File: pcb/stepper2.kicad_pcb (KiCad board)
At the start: 2 copper layers, 92 x 138 mm, 52 parts, among them J1 DA15_Receptacle_MountingHoles, J10 Conn_01x07_Pin, J11 FAN, J2 DA15_Receptacle_MountingHoles, J3 DA15_Receptacle_MountingHoles, J4 DE15_Receptacle_HighDensity, J5 DE15_Receptacle_HighDensity, J6 DE15_Receptacle_HighDensity, J7 Conn_01x04_Pin, J8 Conn_01x05_Pin, J9 Conn_01x06_Pin, SW1 SW_Push, SW2 SW_Push, SW3 SW_Push, SW4 SW_Push, SW5 SW_Push, SW6 SW_Push, U1 AM26LS32ACN, U2 AM26LS32Ax, U3 AM26LS32ACN, U4 TMC2209_BIGTREETECH, U5 TMC2209_BIGTREETECH, U6 TMC2209_BIGTREETECH

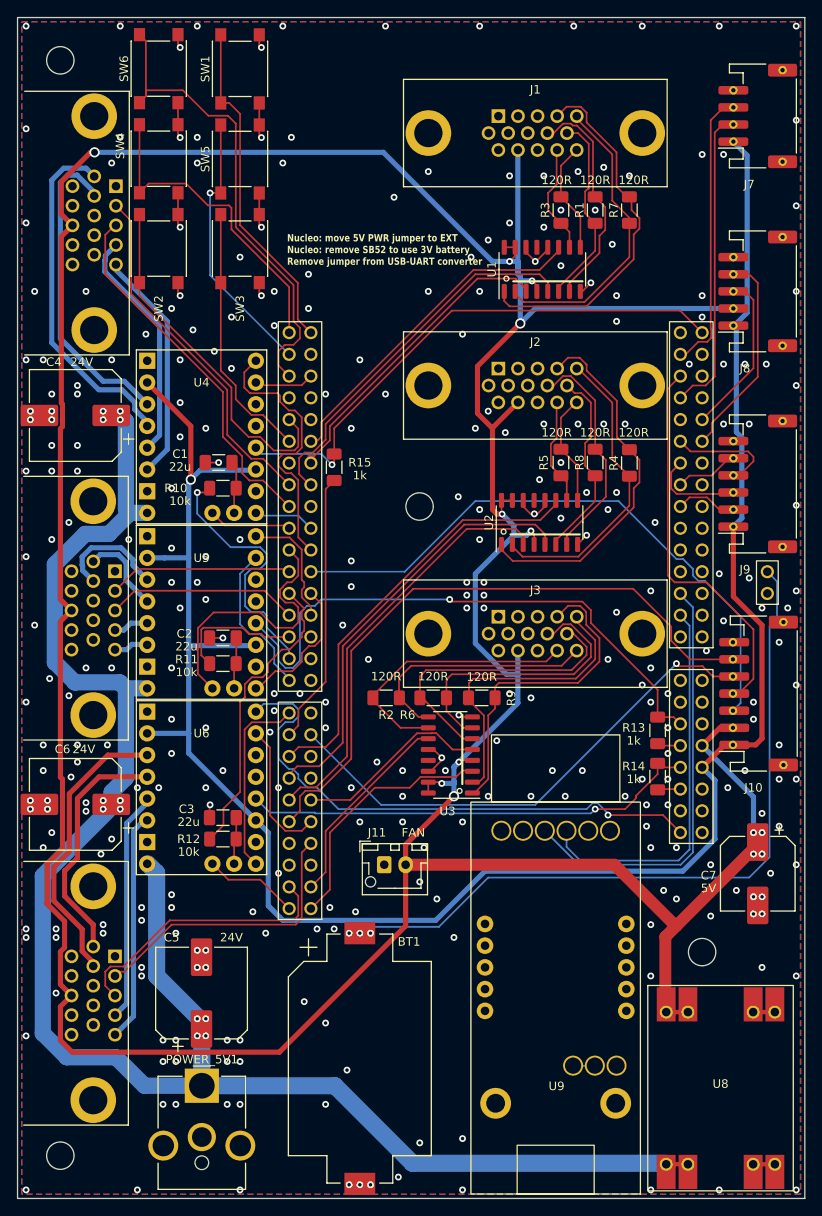
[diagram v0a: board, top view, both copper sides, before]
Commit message: PCB - adjustments and author/date label
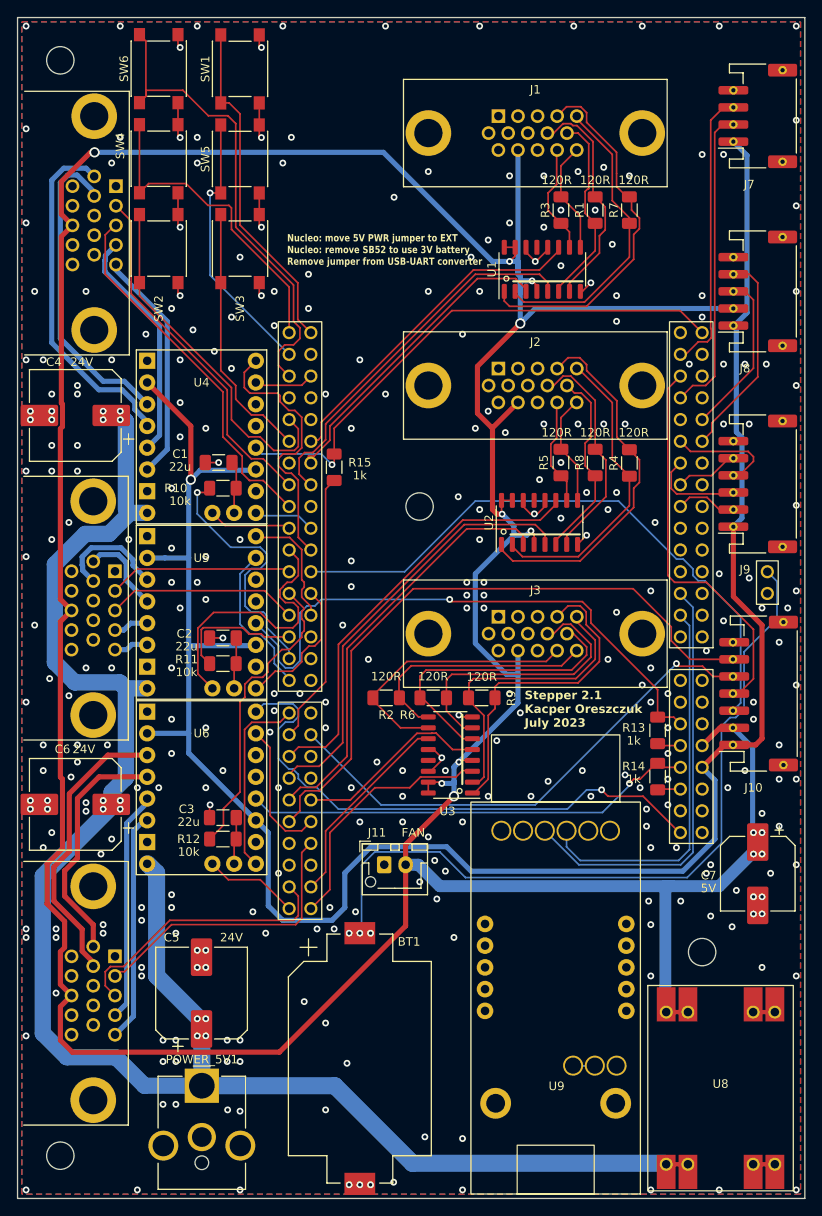
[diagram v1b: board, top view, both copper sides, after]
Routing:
- net +3V3: track 240.5 -> 245.2 mm
- net VBAT: track 88.4 -> 91.8 mm
- net +5V: track 456.3 -> 459.6 mm
- net DIR3: track 64.4 -> 65.5 mm
- net TMCUART3: track 53.9 -> 53.0 mm
- net GND: vias 307 -> 311
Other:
- board text added: "Stepper 2.1 Kacper Oreszczuk July 2023"

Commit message: PCB - minor tweaks
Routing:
- net +5V: track 459.6 -> 458.4 mm
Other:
- board text added: "Remove jumper from USB-UART converter Nucleo: move 5V PWR jumper to EXT Nucleo: remove SB52 to use 3V battery"
- board text removed: "Nucleo: move 5V PWR jumper to EXT Nucleo: remove SB52 to use 3V battery Remove jumper from USB-UART converter"
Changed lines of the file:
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@@
     (property "ki_keywords" "R res resistor")
     (attr smd)
-    (fp_text reference "R5" (at 0 -2 270) (layer "F.SilkS")
+    (fp_text reference "R5" (at 1.5 -3.25) (layer "F.SilkS")
         (effects (font (size 1 1) (thickness 0.15)))
     )
-    (fp_text value "120R" (at 3.5 -0.5 180) (layer "F.SilkS")
+    (fp_text value "120R" (at 0 -3.25 180) (layer "F.SilkS")
         (effects (font (size 1 1) (thickness 0.15)))
     )
@@
     (property "ki_keywords" "R res resistor")
     (attr smd)
-    (fp_text reference "R7" (at 0 -1.82 90) (layer "F.SilkS")
+    (fp_text reference "R7" (at 1.25 3.25 180) (layer "F.SilkS")
         (effects (font (size 1 1) (thickness 0.15)))
     )
-    (fp_text value "120R" (at 3.5 0.5 180) (layer "F.SilkS")
+    (fp_text value "120R" (at -0.5 3.25 180) (layer "F.SilkS")
         (effects (font (size 1 1) (thickness 0.15)))
     )
@@
         (effects (font (size 1 1) (thickness 0.15)))
     )
-    (fp_text value "120R" (at 3.5 0 180) (layer "F.SilkS")
+    (fp_text value "120R" (at 0 2 270) (layer "F.SilkS")
         (effects (font (size 1 1) (thickness 0.15)))
     )
@@
     (property "ki_keywords" "R res resistor")
     (attr smd)
-    (fp_text reference "R2" (at 0 2) (layer "F.SilkS")
+    (fp_text reference "R2" (at -4.075 -2) (layer "F.SilkS")
         (effects (font (size 1 1) (thickness 0.15)))
     )
-    (fp_text value "120R" (at 0 -2.5) (layer "F.SilkS")
+    (fp_text value "120R" (at -4.075 -0.5) (layer "F.SilkS")
         (effects (font (size 1 1) (thickness 0.15)))
     )
@@
     (property "ki_keywords" "R res resistor")
     (attr smd)
-    (fp_text reference "R9" (at 3.45 0.05 90) (layer "F.SilkS")
+    (fp_text reference "R9" (at 2.25 1.75 180) (layer "F.SilkS")
         (effects (font (size 1 1) (thickness 0.15)))
     )
-    (fp_text value "120R" (at 0 -2.45) (layer "F.SilkS")
+    (fp_text value "120R" (at 2.25 3.25) (layer "F.SilkS")
         (effects (font (size 1 1) (thickness 0.15)))
     )
@@
     (property "ki_keywords" "R res resistor")
     (attr smd)
-    (fp_text reference "R3" (at 0 -1.82 90) (layer "F.SilkS")
+    (fp_text reference "R3" (at 1.75 -3.25 180) (layer "F.SilkS")
         (effects (font (size 1 1) (thickness 0.15)))
     )
-    (fp_text value "120R" (at 3.5 -0.5 180) (layer "F.SilkS")
+    (fp_text value "120R" (at 0 -3.25 180) (layer "F.SilkS")
         (effects (font (size 1 1) (thickness 0.15)))
     )
@@
     (property "ki_keywords" "R res resistor")
     (attr smd)
-    (fp_text reference "R6" (at -3 2) (layer "F.SilkS")
+    (fp_text reference "R6" (at -3.325 2) (layer "F.SilkS")
         (effects (font (size 1 1) (thickness 0.15)))
     )
-    (fp_text value "120R" (at 0 -2.5) (layer "F.SilkS")
+    (fp_text value "120R" (at -3.575 3.25) (layer "F.SilkS")
         (effects (font (size 1 1) (thickness 0.15)))
     )
@@
     (property "ki_keywords" "R res resistor")
     (attr smd)
-    (fp_text reference "R4" (at 0 -1.82 90) (layer "F.SilkS")
+    (fp_text reference "R4" (at -3.2 1.75 180) (layer "F.SilkS")
         (effects (font (size 1 1) (thickness 0.15)))
     )
-    (fp_text value "120R" (at 3.55 0.5 180) (layer "F.SilkS")
+    (fp_text value "120R" (at -4.7 2 180) (layer "F.SilkS")
         (effects (font (size 1 1) (thickness 0.15)))
     )
@@
     (property "ki_keywords" "R res resistor")
     (attr smd)
-    (fp_text reference "R8" (at 0 -1.82 90) (layer "F.SilkS")
+    (fp_text reference "R8" (at -3.5 0.75 180) (layer "F.SilkS")
         (effects (font (size 1 1) (thickness 0.15)))
     )
-    (fp_text value "120R" (at 3.5 0 180) (layer "F.SilkS")
+    (fp_text value "120R" (at -5 0.75) (layer "F.SilkS")
         (effects (font (size 1 1) (thickness 0.15)))
     )
@@
   (gr_line (start 0 138) (end 0 0)
     (stroke (width 0.1) (type default)) (layer "Edge.Cuts"))
-  (gr_text "Nucleo: move 5V PWR jumper to EXT\nNucleo: remove SB52 to use 3V battery\nRemove jumper from USB-UART converter" (at 31.5 29) (layer "F.SilkS")
-    (effects (font (size 0.85 0.7) (thickness 0.175) bold) (justify left bottom))
+  (gr_text "Remove jumper from USB-UART converter\nNucleo: move 5V PWR jumper to EXT\nNucleo: remove SB52 to use 3V battery" (at 30 28.5) (layer "F.SilkS")
+    (effects (font (size 0.85 0.85) (thickness 0.175) bold) (justify left bottom))
   )
   (gr_text "Stepper 2.1\nKacper Oreszczuk\nJuly 2023" (at 59.25 83) (layer "F.SilkS")
@@
   (via (at 18.5 107) (size 0.8) (drill 0.4) (layers "F.Cu" "B.Cu") (free) (net 2))
   (via (at 82 137) (size 0.8) (drill 0.4) (layers "F.Cu" "B.Cu") (free) (net 2))
-  (via (at 69 57.5) (size 0.8) (drill 0.4) (layers "F.Cu" "B.Cu") (free) (net 2))
+  (via (at 69 58.25) (size 0.8) (drill 0.4) (layers "F.Cu" "B.Cu") (free) (net 2))
   (via (at 11 40) (size 0.8) (drill 0.4) (layers "F.Cu" "B.Cu") (free) (net 2))
   (via (at 85.5 47.5) (size 0.8) (drill 0.4) (layers "F.Cu" "B.Cu") (free) (net 2))
@@
   (via (at 26 61) (size 0.8) (drill 0.4) (layers "F.Cu" "B.Cu") (free) (net 2))
   (via (at 28.5 24.5) (size 0.8) (drill 0.4) (layers "F.Cu" "B.Cu") (net 2))
-  (via (at 53 28) (size 0.8) (drill 0.4) (layers "F.Cu" "B.Cu") (free) (net 2))
+  (via (at 52.25 29) (size 0.8) (drill 0.4) (layers "F.Cu" "B.Cu") (free) (net 2))
   (via (at 82.5 16) (size 0.8) (drill 0.4) (layers "F.Cu" "B.Cu") (free) (net 2))
   (via (at 6.25 88.75) (size 0.8) (drill 0.4) (layers "F.Cu" "B.Cu") (free) (net 2))
@@
   (via (at 18 55) (size 0.8) (drill 0.4) (layers "F.Cu" "B.Cu") (free) (net 2))
   (via (at 1 63) (size 0.8) (drill 0.4) (layers "F.Cu" "B.Cu") (free) (net 2))
-  (via (at 55 26) (size 0.8) (drill 0.4) (layers "F.Cu" "B.Cu") (free) (net 2))
+  (via (at 55.5 26.75) (size 0.8) (drill 0.4) (layers "F.Cu" "B.Cu") (free) (net 2))
   (via (at 54 61) (size 0.8) (drill 0.4) (layers "F.Cu" "B.Cu") (free) (net 2))
   (via (at 4 50) (size 0.8) (drill 0.4) (layers "F.Cu" "B.Cu") (free) (net 2))
@@
   (segment (start 62 22.55) (end 63.5 24.05) (width 0.2) (layer "F.Cu") (net 36))
   (segment (start 64.5 25.05) (end 63.5 24.05) (width 0.2) (layer "F.Cu") (net 36))
-  (segment (start 65.77 26.85) (end 65.77 23.22) (width 0.2) (layer "F.Cu") (net 37))
+  (segment (start 65.25 24) (end 65.25 22.5) (width 0.2) (layer "F.Cu") (net 37))
   (segment (start 63.5 20.95) (end 63.5 17.325001) (width 0.2) (layer "F.Cu") (net 37))
-  (segment (start 65.77 23.22) (end 63.5 20.95) (width 0.2) (layer "F.Cu") (net 37))
+  (segment (start 65.77 26.85) (end 65.77 24.52) (width 0.2) (layer "F.Cu") (net 37))
+  (segment (start 65.77 24.52) (end 65.25 24) (width 0.2) (layer "F.Cu") (net 37))
+  (segment (start 65.25 22.5) (end 63.7 20.95) (width 0.2) (layer "F.Cu") (net 37))
+  (segment (start 63.7 20.95) (end 63.5 20.95) (width 0.2) (layer "F.Cu") (net 37))
   (segment (start 63.5 17.325001) (end 65.345001 15.48) (width 0.2) (layer "F.Cu") (net 37))
   (segment (start 72 55) (end 72 57.25) (width 0.2) (layer "F.Cu") (net 38))
@@
   (segment (start 51.765 86.81) (end 51.575 87) (width 0.2) (layer "F.Cu") (net 142))
   (segment (start 56.0255 58.0255) (end 55.5 57.5) (width 0.6) (layer "F.Cu") (net 142))
-  (segment (start 86.5 96.35) (end 86.5 96.628882) (width 1.4) (layer "F.Cu") (net 142))
   (segment (start 58.15 27.85) (end 58.15 26.85) (width 0.2) (layer "F.Cu") (net 142))
   (segment (start 53.15 86.81) (end 51.765 86.81) (width 0.2) (layer "F.Cu") (net 142))
@@
   (segment (start 60.69 32) (end 60.69 31.336602) (width 0.2) (layer "F.Cu") (net 142))
   (segment (start 5.00772 70.585) (end 5.00772 88.75386) (width 0.6) (layer "F.Cu") (net 142))
-  (segment (start 75.7 116.12) (end 75.8 116.22) (width 1.4) (layer "F.Cu") (net 142))
   (segment (start 53.745001 46.245001) (end 53.745001 40.754999) (width 0.6) (layer "F.Cu") (net 142))
   (segment (start 5.12 25.585) (end 5.12 45.05934) (width 0.6) (layer "F.Cu") (net 142))
@@
   (via (at 58.75 35.75) (size 1.2) (drill 0.8) (layers "F.Cu" "B.Cu") (net 142))
   (segment (start 58.475001 28.5) (end 58.475001 29.975001) (width 0.6) (layer "B.Cu") (net 142))
-  (segment (start 76.5 101.5) (end 75.7 101.5) (width 1.4) (layer "B.Cu") (net 142))
   (segment (start 57.116523 76.75) (end 53.5 73.133477) (width 0.6) (layer "B.Cu") (net 142))
   (segment (start 58.75 32.152398) (end 58.75 30.25) (width 0.6) (layer "B.Cu") (net 142))

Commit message: PCB - final version sent to JLCPCB
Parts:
- U4: value TMC2209_BIGTREETECH -> TMC2226_BIGTREETECH
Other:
- board text added: "JLCJLCJLCJLC"
- board text added: "Remove jumper from USB-UART converter Unsolder potentiometer from TMC drivers Nucleo: move 5V PWR jumper to EXT Nucleo: remove SB52 to use 3V battery"
- board text added: "Stepper 2.1.0 Kacper Oreszczuk July 2023"
- board text removed: "Remove jumper from USB-UART converter Nucleo: move 5V PWR jumper to EXT Nucleo: remove SB52 to use 3V battery"
- board text removed: "Stepper 2.1 Kacper Oreszczuk July 2023"
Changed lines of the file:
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@@
       (polygon
         (pts
-          (xy 73.55 113.91)
-          (xy 90.75 113.91)
-          (xy 90.75 136.31)
-          (xy 73.55 136.31)
+          (xy 73.26 113.68)
+          (xy 91.04 113.68)
+          (xy 91.04 136.54)
+          (xy 73.26 136.54)
         )
       )
@@
       (polygon
         (pts
-          (xy 72.885 138.278)
-          (xy 52.885 138.278)
-          (xy 52.885 91.578)
-          (xy 72.885 91.578)
+          (xy 73.045 138.48)
+          (xy 52.725 138.48)
+          (xy 52.725 91.49)
+          (xy 73.045 91.49)
         )
       )
@@
     (property "ki_keywords" "receiver rs485 rs422 differential")
     (attr smd)
-    (fp_text reference "U3" (at 0.325 -6.575) (layer "F.SilkS")
+    (fp_text reference "U3" (at 5.075 -0.575) (layer "F.SilkS")
         (effects (font (size 1 1) (thickness 0.15)))
     )
@@
     (property "ki_keywords" "switch normally-open pushbutton push-button")
     (attr smd)
-    (fp_text reference "SW3" (at -7 0 90) (layer "F.SilkS")
+    (fp_text reference "SW3" (at 0 -4 90) (layer "F.SilkS")
         (effects (font (size 1 1) (thickness 0.15)))
     )
@@
     (property "ki_keywords" "R res resistor")
     (attr smd)
-    (fp_text reference "R1" (at 0 -1.82 90) (layer "F.SilkS")
+    (fp_text reference "R1" (at -3 0.75 180) (layer "F.SilkS")
         (effects (font (size 1 1) (thickness 0.15)))
     )
-    (fp_text value "120R" (at 0 2 270) (layer "F.SilkS")
+    (fp_text value "120R" (at -4.5 1) (layer "F.SilkS")
         (effects (font (size 1 1) (thickness 0.15)))
     )
@@
     (property "ki_keywords" "switch normally-open pushbutton push-button")
     (attr smd)
-    (fp_text reference "SW2" (at -7 0 90) (layer "F.SilkS")
+    (fp_text reference "SW2" (at 0 4 90) (layer "F.SilkS")
         (effects (font (size 1 1) (thickness 0.15)))
     )
@@
         (effects (font (size 1 1) (thickness 0.1)))
     )
-    (fp_text value "TMC2209_BIGTREETECH" (at 0 -11.43 unlocked) (layer "F.Fab")
-        (effects (font (size 1 1) (thickness 0.15)))
+    (fp_text value "TMC2226_BIGTREETECH" (at 0 -11 unlocked) (layer "F.SilkS")
+        (effects (font (size 0.9 0.9) (thickness 0.15)))
     )
     (fp_text user "${REFERENCE}" (at 0 -8.89 unlocked) (layer "F.Fab")
@@
     (property "ki_keywords" "cap capacitor")
     (attr smd)
-    (fp_text reference "C7" (at 0.2 5.75 -180) (layer "F.SilkS")
+    (fp_text reference "C7" (at 1.2 5.75 -180) (layer "F.SilkS")
         (effects (font (size 1 1) (thickness 0.15)))
     )
-    (fp_text value "5V" (at 1.7 5.75 -180) (layer "F.SilkS")
+    (fp_text value "5V" (at 2.95 5.75 -180) (layer "F.SilkS")
         (effects (font (size 1 1) (thickness 0.15)))
     )
@@
     (property "ki_keywords" "switch normally-open pushbutton push-button")
     (attr smd)
-    (fp_text reference "SW4" (at 1.5 -4.5 90) (layer "F.SilkS")
+    (fp_text reference "SW4" (at 0 4 90) (layer "F.SilkS")
         (effects (font (size 1 1) (thickness 0.15)))
     )
@@
     (property "ki_keywords" "cap capacitor")
     (attr smd)
-    (fp_text reference "C6" (at 1.5 6.448) (layer "F.SilkS")
+    (fp_text reference "C6" (at 2 6.448) (layer "F.SilkS")
         (effects (font (size 1 1) (thickness 0.15)))
     )
-    (fp_text value "24V" (at -1 6.448) (layer "F.SilkS")
+    (fp_text value "24V" (at -1.25 6.448) (layer "F.SilkS")
         (effects (font (size 1 1) (thickness 0.15)))
     )
@@
     (property "ki_keywords" "R res resistor")
     (attr smd)
-    (fp_text reference "R14" (at -1.2 2.8) (layer "F.SilkS")
+    (fp_text reference "R14" (at -1.7 2.55) (layer "F.SilkS")
         (effects (font (size 1 1) (thickness 0.15)))
     )
-    (fp_text value "1k" (at 0.3 2.8 -180) (layer "F.SilkS")
+    (fp_text value "1k" (at -0.2 2.55 -180) (layer "F.SilkS")
         (effects (font (size 1 1) (thickness 0.15)))
     )
@@
     (property "ki_keywords" "switch normally-open pushbutton push-button")
     (attr smd)
-    (fp_text reference "SW6" (at 0 -4.05 90) (layer "F.SilkS")
+    (fp_text reference "SW6" (at -0.025 4 90) (layer "F.SilkS")
         (effects (font (size 1 1) (thickness 0.15)))
     )
@@
   (gr_line (start 0 138) (end 0 0)
     (stroke (width 0.1) (type default)) (layer "Edge.Cuts"))
-  (gr_text "Remove jumper from USB-UART converter\nNucleo: move 5V PWR jumper to EXT\nNucleo: remove SB52 to use 3V battery" (at 30 28.5) (layer "F.SilkS")
-    (effects (font (size 0.85 0.85) (thickness 0.175) bold) (justify left bottom))
+  (gr_text "Remove jumper from USB-UART converter\nUnsolder potentiometer from TMC drivers\nNucleo: move 5V PWR jumper to EXT\nNucleo: remove SB52 to use 3V battery" (at 29.5 28.25) (layer "F.SilkS")
+    (effects (font (size 0.85 0.85) (thickness 0.15) bold) (justify left bottom))
+  )
+  (gr_text "Stepper 2.1.0\nKacper Oreszczuk\nJuly 2023" (at 31 7.5) (layer "F.SilkS")
+    (effects (font (size 1.2 1.2) (thickness 0.25) bold) (justify left bottom))
   )
-  (gr_text "Stepper 2.1\nKacper Oreszczuk\nJuly 2023" (at 59.25 83) (layer "F.SilkS")
-    (effects (font (size 1 1) (thickness 0.25) bold) (justify left bottom))
+  (gr_text "JLCJLCJLCJLC" (at 57.75 101.25) (layer "F.SilkS")
+    (effects (font (size 1 1) (thickness 0.2) bold) (justify left bottom))
   )
   (segment (start 25.5625 75.4875) (end 25.55 75.5) (width 0.2) (layer "F.Cu") (net 1))
@@
   (via (at 4.5 107.5) (size 0.8) (drill 0.4) (layers "F.Cu" "B.Cu") (free) (net 2))
   (via (at 73.75 103.25) (size 0.8) (drill 0.4) (layers "F.Cu" "B.Cu") (free) (net 2))
-  (via (at 21 17) (size 0.8) (drill 0.4) (layers "F.Cu" "B.Cu") (free) (net 2))
+  (via (at 21.25 18.5) (size 0.8) (drill 0.4) (layers "F.Cu" "B.Cu") (free) (net 2))
   (via (at 52 94) (size 0.8) (drill 0.4) (layers "F.Cu" "B.Cu") (free) (net 2))
   (via (at 89 89) (size 0.8) (drill 0.4) (layers "F.Cu" "B.Cu") (free) (net 2))
@@
   (via (at 91 137) (size 0.8) (drill 0.4) (layers "F.Cu" "B.Cu") (free) (net 2))
   (via (at 18 104) (size 0.8) (drill 0.4) (layers "F.Cu" "B.Cu") (free) (net 2))
-  (via (at 15 37) (size 0.8) (drill 0.4) (layers "F.Cu" "B.Cu") (free) (net 2))
+  (via (at 15 36.25) (size 0.8) (drill 0.4) (layers "F.Cu" "B.Cu") (free) (net 2))
   (via (at 80.5 100) (size 0.8) (drill 0.4) (layers "F.Cu" "B.Cu") (free) (net 2))
   (via (at 33 79) (size 0.8) (drill 0.4) (layers "F.Cu" "B.Cu") (free) (net 2))
@@
   (via (at 28.5 32.5) (size 0.8) (drill 0.4) (layers "F.Cu" "B.Cu") (net 2))
   (via (at 82.5 47.5) (size 0.8) (drill 0.4) (layers "F.Cu" "B.Cu") (free) (net 2))
-  (via (at 73.5 92.5) (size 0.8) (drill 0.4) (layers "F.Cu" "B.Cu") (free) (net 2))
+  (via (at 73.5 92.75) (size 0.8) (drill 0.4) (layers "F.Cu" "B.Cu") (free) (net 2))
   (via (at 63.5 52) (size 0.8) (drill 0.4) (layers "F.Cu" "B.Cu") (free) (net 2))
   (via (at 4 46) (size 0.8) (drill 0.4) (layers "F.Cu" "B.Cu") (net 2))
@@
   (via (at 44 21) (size 0.8) (drill 0.4) (layers "F.Cu" "B.Cu") (free) (net 2))
   (via (at 52 131) (size 0.8) (drill 0.4) (layers "F.Cu" "B.Cu") (free) (net 2))
-  (via (at 69.5 26.5) (size 0.8) (drill 0.4) (layers "F.Cu" "B.Cu") (free) (net 2))
+  (via (at 69.75 25.75) (size 0.8) (drill 0.4) (layers "F.Cu" "B.Cu") (free) (net 2))
   (via (at 10 107) (size 0.8) (drill 0.4) (layers "F.Cu" "B.Cu") (free) (net 2))
   (via (at 77.5 103.25) (size 0.8) (drill 0.4) (layers "F.Cu" "B.Cu") (free) (net 2))
@@
   (segment (start 26.525 83.207233) (end 26.525 97.565) (width 0.2) (layer "F.Cu") (net 120))
   (segment (start 27.372233 82.36) (end 26.525 83.207233) (width 0.2) (layer "F.Cu") (net 120))
-  (segment (start 68.25 90.25) (end 69 91) (width 0.2) (layer "F.Cu") (net 121))
-  (segment (start 77.34 95.24) (end 77.46 95.24) (width 0.2) (layer "F.Cu") (net 121))
-  (segment (start 69 91) (end 73.1 91) (width 0.2) (layer "F.Cu") (net 121))
-  (segment (start 73.1 91) (end 77.34 95.24) (width 0.2) (layer "F.Cu") (net 121))
+  (segment (start 68.25 90.25) (end 69.25 91.25) (width 0.2) (layer "F.Cu") (net 121))
+  (segment (start 76.99 95.24) (end 77.46 95.24) (width 0.2) (layer "F.Cu") (net 121))
+  (segment (start 69.25 91.25) (end 73 91.25) (width 0.2) (layer "F.Cu") (net 121))
+  (segment (start 73 91.25) (end 76.99 95.24) (width 0.2) (layer "F.Cu") (net 121))
   (via (at 68.25 90.25) (size 0.8) (drill 0.4) (layers "F.Cu" "B.Cu") (net 121))
   (segment (start 28.76 80.2) (end 27.85 81.11) (width 0.2) (layer "B.Cu") (net 121))
